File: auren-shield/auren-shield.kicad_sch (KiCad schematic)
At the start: 47 parts, among them J1 Tympan_SJ-3523-SMT-TR, J2 Tympan_SJ-3524-SMT-TR-PI, J3 HDMI_A_Molex_208658-1001, J5 Conn_01x01, J6 Conn_01x01, P1 CONN_01X06, P2 CONN_01X06, P3 CONN_01X06, P4 CONN_01X06, P5 CONN_01X06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

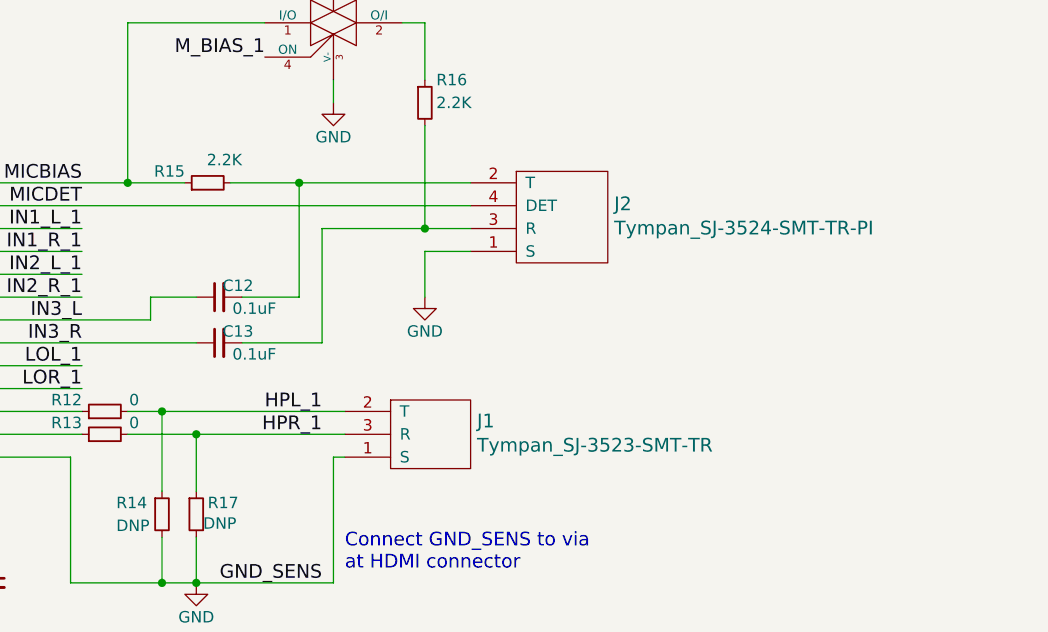
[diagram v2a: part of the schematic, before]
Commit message: Removed audio jacks. Resized PCB
Cleaned up around GND_SNS circuit
PCB is now 38mm x 40mm (was x 44mm)
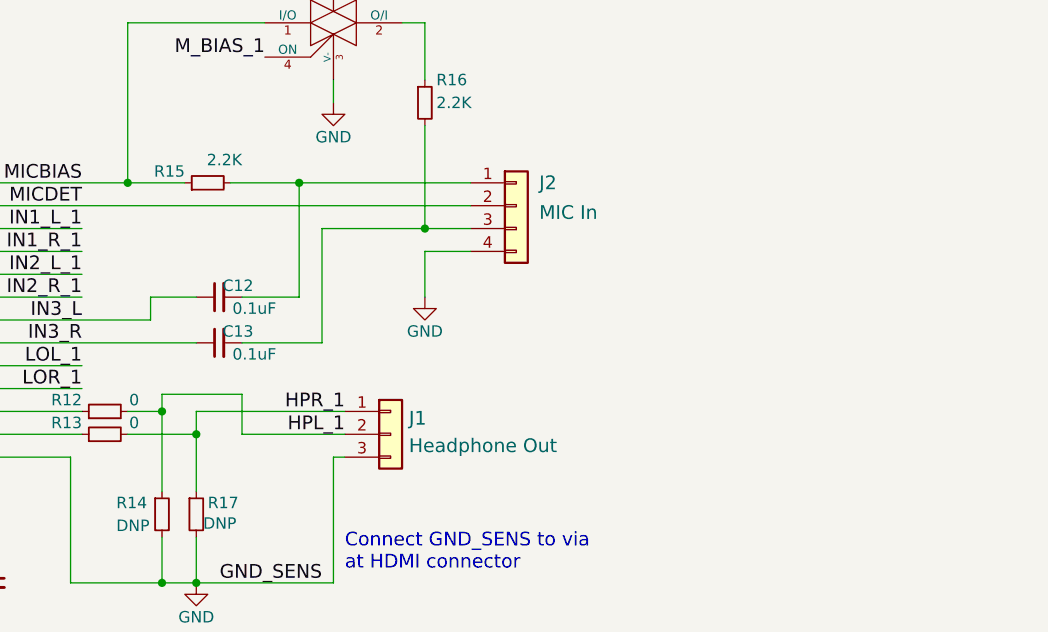
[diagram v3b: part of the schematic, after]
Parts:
- C23: footprint Capacitors_SMD:C_0402 -> Capacitor_SMD:C_0402_1005Metric
- J1: value Tympan_SJ-3523-SMT-TR -> Headphone Out; footprint Tympan:SJ-3523-SMT-TR -> Connector_PinHeader_2.54mm:PinHeader_1x03_P2.54mm_Vertical; symbol auren-shield:Tympan_SJ-3523-SMT-TR -> Connector_Generic:Conn_01x03
- J2: value Tympan_SJ-3524-SMT-TR-PI -> MIC In; footprint Tympan:SJ-3524-SMT-TR -> Connector_PinHeader_2.54mm:PinHeader_1x04_P2.54mm_Vertical; symbol auren-shield:Tympan_SJ-3524-SMT-TR-PI -> Connector_Generic:Conn_01x04
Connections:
- net GND: now also J1.3 (Pin_3), J2.4 (Pin_4); no longer J1.1 (S), J2.1 (S)
- net HPR_1: now also J1.1 (Pin_1); no longer J1.3 (R)
- net MICDET: now also J2.2 (Pin_2); no longer J2.4 (DET)
- net at C12.2, R15.2: now also J2.1 (Pin_1); no longer J2.2 (T)
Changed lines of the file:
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@@
 	)
 	(junction
-		(at 162.56 82.55)
-		(diameter 0)
-		(color 0 0 0 0)
-	)
-	(junction
 		(at 115.57 99.06)
 		(diameter 0)
@@
 	)
 	(junction
-		(at 111.76 99.06)
+		(at 162.56 82.55)
 		(diameter 0)
 		(color 0 0 0 0)
 	)
 	(junction
-		(at 109.22 99.06)
+		(at 111.76 99.06)
 		(diameter 0)
 		(color 0 0 0 0)
@@
 	)
 	(junction
+		(at 109.22 99.06)
+		(diameter 0)
+		(color 0 0 0 0)
+	)
+	(junction
 		(at 162.56 99.06)
 		(diameter 0)
@@
 	(wire
 		(pts
+			(xy 179.07 80.01) (xy 162.56 80.01)
+		)
+		(stroke
+			(width 0)
+			(type default)
+		)
+	)
+	(wire
+		(pts
 			(xy 69.85 69.85) (xy 83.82 69.85)
 		)
@@
 	(wire
 		(pts
-			(xy 110.49 43.18) (xy 113.03 43.18)
+			(xy 167.64 82.55) (xy 167.64 78.105)
 		)
 		(stroke
@@
 	(wire
 		(pts
-			(xy 39.37 72.39) (xy 25.4 72.39)
+			(xy 110.49 43.18) (xy 113.03 43.18)
 		)
 		(stroke
@@
 	(wire
 		(pts
-			(xy 247.65 135.89) (xy 245.11 135.89)
+			(xy 39.37 72.39) (xy 25.4 72.39)
 		)
 		(stroke
@@
 	(wire
 		(pts
-			(xy 176.53 59.69) (xy 187.96 59.69)
+			(xy 247.65 135.89) (xy 245.11 135.89)
 		)
 		(stroke
@@
 	(wire
 		(pts
-			(xy 72.39 59.69) (xy 58.42 59.69)
+			(xy 176.53 59.69) (xy 187.96 59.69)
 		)
 		(stroke
@@
 	(wire
 		(pts
-			(xy 92.71 25.4) (xy 86.36 25.4)
+			(xy 72.39 59.69) (xy 58.42 59.69)
 		)
 		(stroke
@@
 	(wire
 		(pts
-			(xy 162.56 82.55) (xy 179.07 82.55)
+			(xy 92.71 25.4) (xy 86.36 25.4)
 		)
 		(stroke
@@
 	(wire
 		(pts
+			(xy 158.75 78.105) (xy 158.75 80.01)
+		)
+		(stroke
+			(width 0)
+			(type default)
+		)
+	)
+	(wire
+		(pts
 			(xy 116.84 148.59) (xy 113.03 148.59)
 		)
@@
 	(wire
 		(pts
+			(xy 167.64 78.105) (xy 158.75 78.105)
+		)
+		(stroke
+			(width 0)
+			(type default)
+		)
+	)
+	(wire
+		(pts
 			(xy 161.29 139.7) (xy 161.29 140.97)
 		)
@@
 	(wire
 		(pts
+			(xy 162.56 80.01) (xy 162.56 82.55)
+		)
+		(stroke
+			(width 0)
+			(type default)
+		)
+	)
+	(wire
+		(pts
 			(xy 177.8 43.18) (xy 177.8 45.72)
 		)
@@
 	(wire
 		(pts
+			(xy 179.07 82.55) (xy 167.64 82.55)
+		)
+		(stroke
+			(width 0)
+			(type default)
+		)
+	)
+	(wire
+		(pts
 			(xy 125.73 30.48) (xy 125.73 33.02)
 		)
@@
 	(wire
 		(pts
-			(xy 158.75 80.01) (xy 179.07 80.01)
-		)
-		(stroke
-			(width 0)
-			(type default)
-		)
-	)
-	(wire
-		(pts
 			(xy 72.39 54.61) (xy 58.42 54.61)
 		)
@@
 	)
 	(label "HPR_1"
-		(at 176.53 82.55 180)
+		(at 179.07 80.01 180)
 		(effects
 			(font
@@
 	)
 	(label "HPL_1"
-		(at 176.53 80.01 180)
+		(at 179.07 82.55 180)
 		(effects
 			(font
@@
 			)
 		)
-		(property "Footprint" "Capacitors_SMD:C_0402"
+		(property "Footprint" "Capacitor_SMD:C_0402_1005Metric"
 			(at 170.18 134.62 0)
 			(effects
@@
 	)
 	(symbol
-		(lib_id "auren-shield:Tympan_SJ-3524-SMT-TR-PI")
-		(at 208.28 59.69 0)
+		(lib_id "Connector_Generic:Conn_01x04")
+		(at 198.12 57.15 0)
 		(unit 1)
 		(exclude_from_sim no)
@@
 		(dnp no)
 		(property "Reference" "J2"
-			(at 208.9912 56.9468 0)
+			(at 200.66 54.61 0)
 			(effects
 				(font
@@
 			)
 		)
-		(property "Value" "Tympan_SJ-3524-SMT-TR-PI"
-			(at 208.9912 59.6392 0)
+		(property "Value" "MIC In"
+			(at 200.66 57.912 0)
 			(effects
 				(font
@@
 			)
 		)
-		(property "Footprint" "Tympan:SJ-3524-SMT-TR"
-			(at 224.282 62.738 0)
+		(property "Footprint" "Connector_PinHeader_2.54mm:PinHeader_1x04_P2.54mm_Vertical"
+			(at 198.12 57.15 0)
 			(effects
 				(font
-					(size 1.524 1.524)
+					(size 1.27 1.27)
 				)
 				(hide yes)
 			)
 		)
-		(property "Datasheet" ""
-			(at 208.28 59.69 0)
+		(property "Datasheet" "~"
+			(at 198.12 57.15 0)
 			(effects
 				(font
-					(size 1.524 1.524)
+					(size 1.27 1.27)
 				)
 				(hide yes)
 			)
 		)
-		(property "Description" ""
-			(at 208.28 59.69 0)
+		(property "Description" "Generic connector, single row, 01x04, script generated (kicad-library-utils/schlib/autogen/connector/)"
+			(at 198.12 57.15 0)
 			(effects
 				(font
@@
 	)
 	(symbol
-		(lib_id "auren-shield:Tympan_SJ-3523-SMT-TR")
-		(at 187.96 82.55 0)
+		(lib_id "Connector_Generic:Conn_01x03")
+		(at 184.15 82.55 0)
 		(unit 1)
 		(exclude_from_sim no)
@@
 		(dnp no)
 		(property "Reference" "J1"
-			(at 193.7512 81.0768 0)
+			(at 186.182 80.772 0)
 			(effects
 				(font
@@
 			)
 		)
-		(property "Value" "Tympan_SJ-3523-SMT-TR"
-			(at 193.7512 83.7692 0)
+		(property "Value" "Headphone Out"
+			(at 186.182 83.82 0)
 			(effects
 				(font
@@
 			)
 		)
-		(property "Footprint" "Tympan:SJ-3523-SMT-TR"
-			(at 213.614 80.264 0)
+		(property "Footprint" "Connector_PinHeader_2.54mm:PinHeader_1x03_P2.54mm_Vertical"
+			(at 184.15 82.55 0)
 			(effects
 				(font
-					(size 1.524 1.524)
+					(size 1.27 1.27)
 				)
 				(hide yes)
 			)
 		)
-		(property "Datasheet" ""
-			(at 187.96 82.55 0)
+		(property "Datasheet" "~"
+			(at 184.15 82.55 0)
 			(effects
 				(font
-					(size 1.524 1.524)
+					(size 1.27 1.27)
 				)
+				(hide yes)
 			)
 		)
-		(property "Description" ""
-			(at 187.96 82.55 0)
+		(property "Description" "Generic connector, single row, 01x03, script generated (kicad-library-utils/schlib/autogen/connector/)"
+			(at 184.15 82.55 0)
 			(effects
 				(font

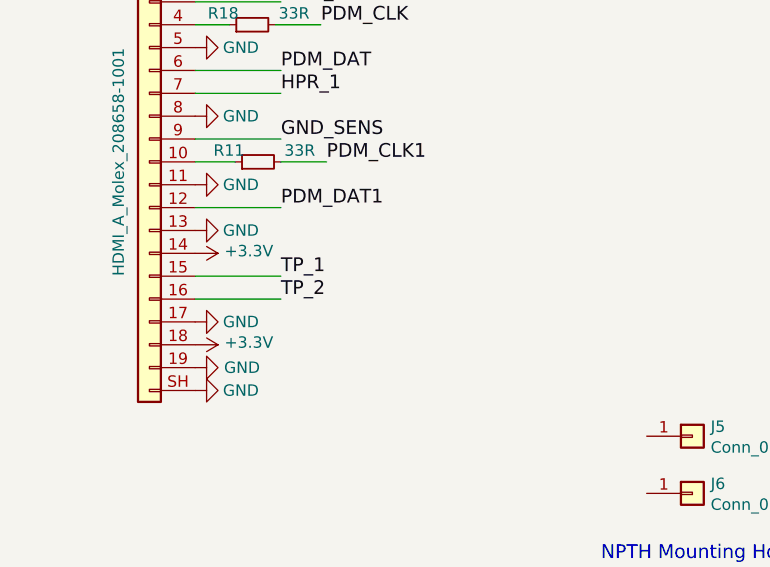
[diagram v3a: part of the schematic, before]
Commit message: Added test point pads
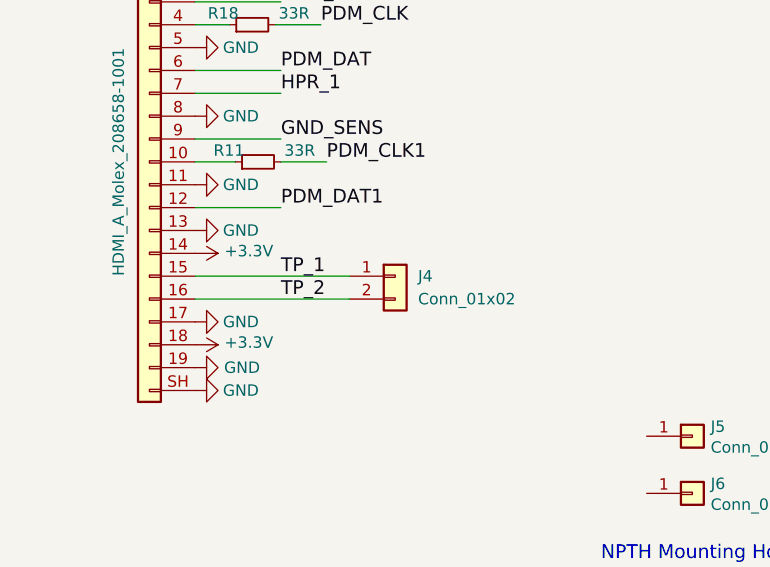
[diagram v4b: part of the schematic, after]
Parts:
- added J4: Conn_01x02, Connector_PinSocket_2.54mm:PinSocket_1x02_P2.54mm_Vertical, symbol Connector_Generic:Conn_01x02
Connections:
- net TP_1: now also J4.1 (Pin_1)
- net TP_2: now also J4.2 (Pin_2)
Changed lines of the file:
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@@
 	(wire
 		(pts
-			(xy 54.61 158.75) (xy 45.085 158.75)
+			(xy 45.085 158.75) (xy 62.23 158.75)
 		)
 		(stroke
@@
 	(wire
 		(pts
-			(xy 54.61 161.29) (xy 45.085 161.29)
+			(xy 45.085 161.29) (xy 62.23 161.29)
 		)
 		(stroke
@@
 					(unit 1)
 				)
+			)
+		)
+	)
+	(symbol
+		(lib_id "Connector_Generic:Conn_01x02")
+		(at 67.31 158.75 0)
+		(unit 1)
+		(exclude_from_sim no)
+		(in_bom yes)
+		(on_board yes)
+		(dnp no)
+		(fields_autoplaced yes)
+		(property "Reference" "J4"
+			(at 69.85 158.7499 0)
+			(effects
+				(font
+					(size 1.27 1.27)
+				)
+				(justify left)
+			)
+		)
+		(property "Value" "Conn_01x02"
+			(at 69.85 161.2899 0)
+			(effects
+				(font
+					(size 1.27 1.27)
+				)
+				(justify left)
+			)
+		)
+		(property "Footprint" "Connector_PinSocket_2.54mm:PinSocket_1x02_P2.54mm_Vertical"
+			(at 67.31 158.75 0)
+			(effects
+				(font
+					(size 1.27 1.27)
+				)
+				(hide yes)
+			)
+		)
+		(property "Datasheet" "~"
+			(at 67.31 158.75 0)
+			(effects
+				(font
+					(size 1.27 1.27)
+				)
+				(hide yes)
+			)
+		)
+		(property "Description" "Generic connector, single row, 01x02, script generated (kicad-library-utils/schlib/autogen/connector/)"
+			(at 67.31 158.75 0)
+			(effects
+				(font
+					(size 1.27 1.27)
+				)
+				(hide yes)
+			)
+		)
+		(pin "1"
+		)
+		(pin "2"
+		)
+		(instances
+			(project ""
+				(path "/2aef2ae4-0dbd-424b-8fd8-1bf240a2e15b"
+					(reference "J4")
+					(unit 1)
+				)

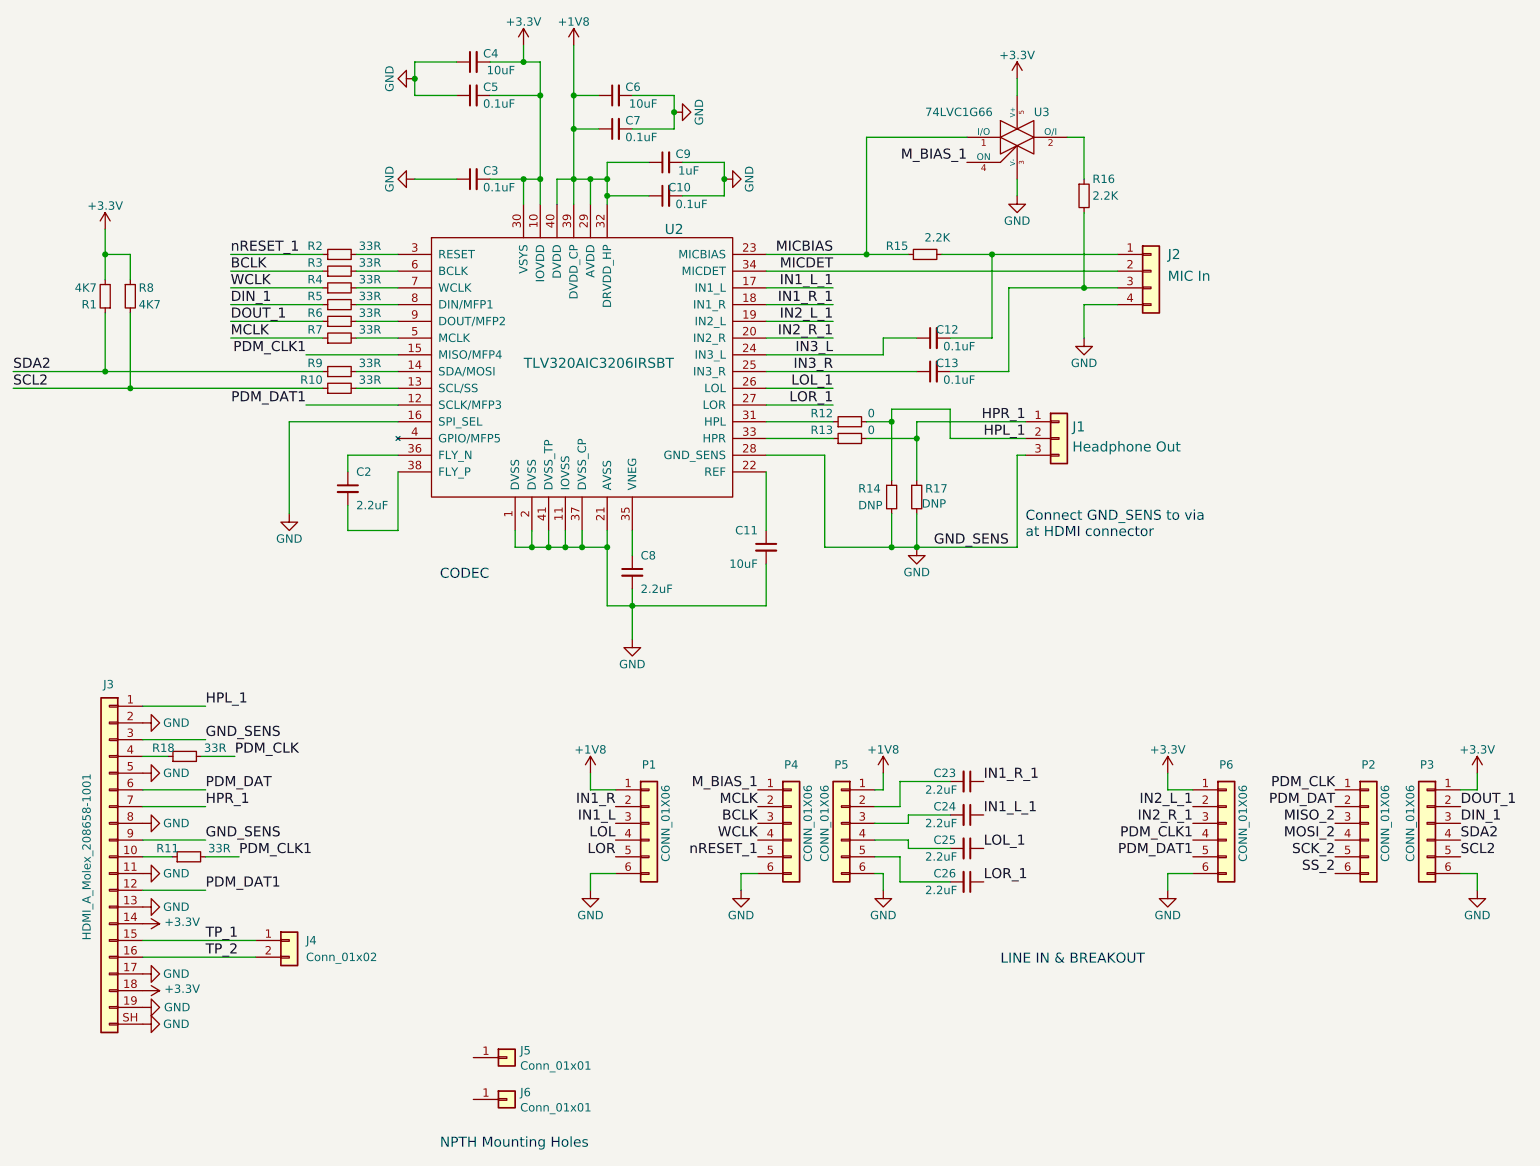
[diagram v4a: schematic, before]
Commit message: Added a step file of the Auren Shield
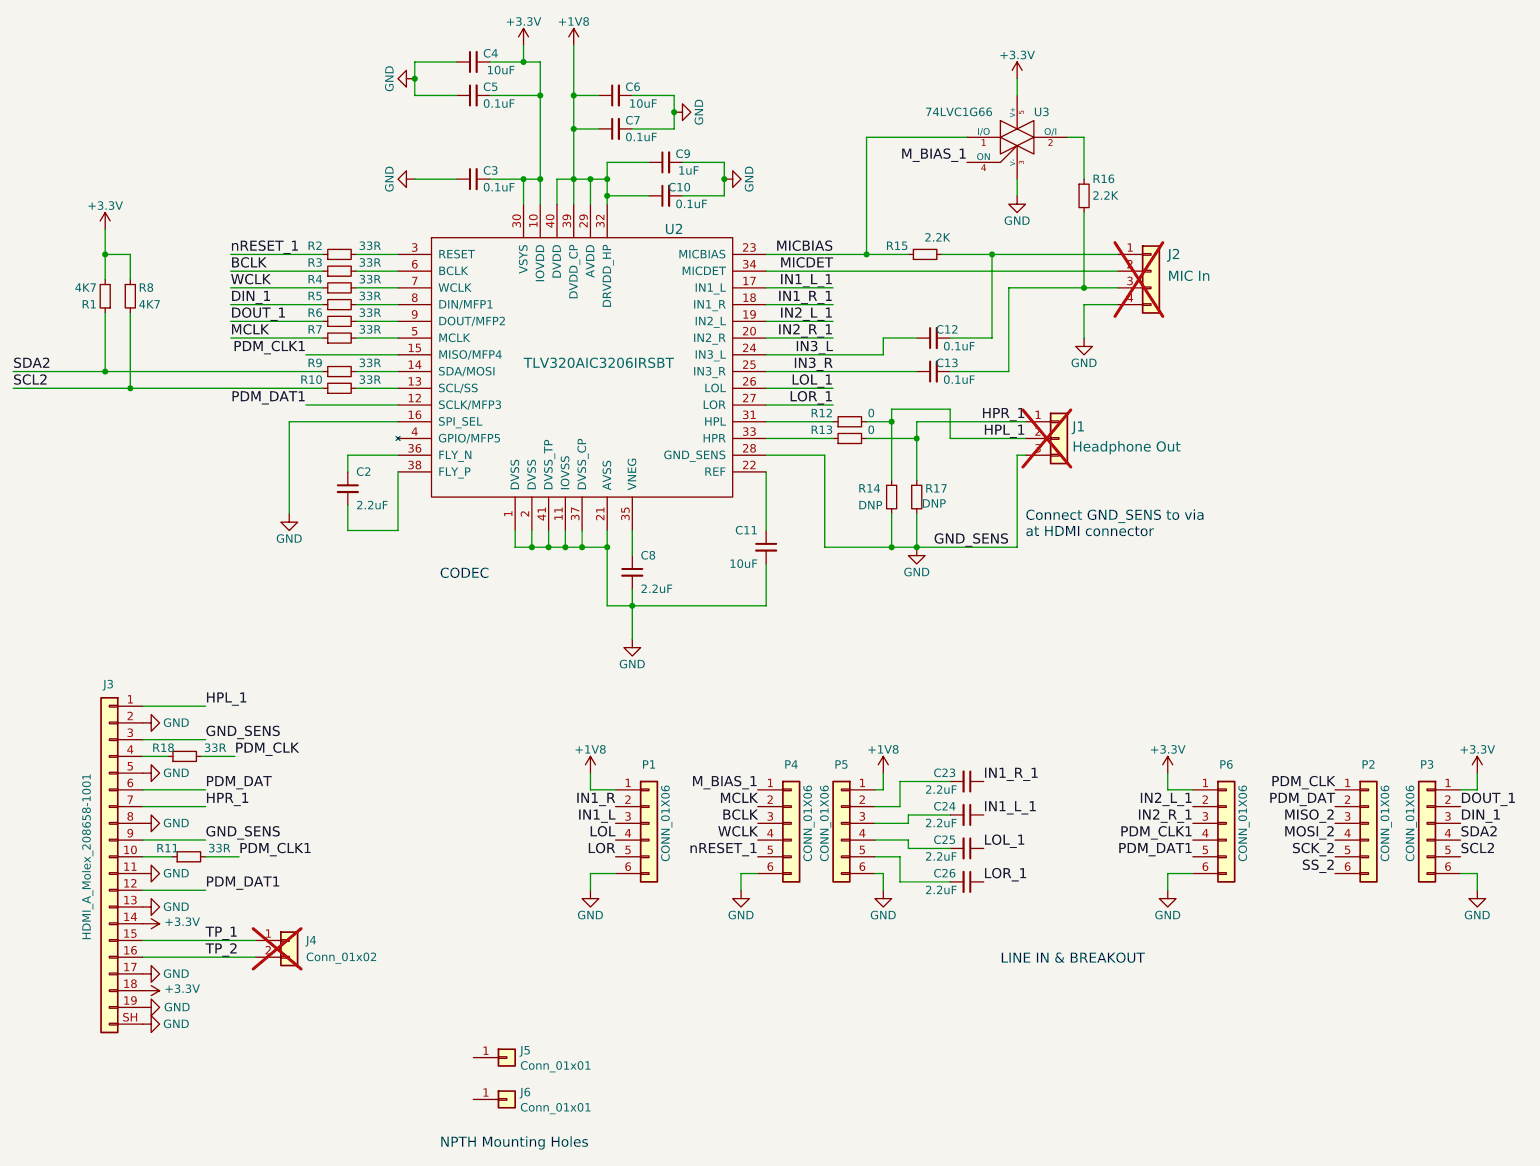
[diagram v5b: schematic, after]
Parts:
- J1, J2, J4: now not fitted; now left out of the parts list
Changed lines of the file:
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@@
 		(unit 1)
 		(exclude_from_sim no)
-		(in_bom yes)
-		(on_board yes)
-		(dnp no)
+		(in_bom no)
+		(on_board yes)
+		(dnp yes)
 		(property "Reference" "J2"
 			(at 200.66 54.61 0)
@@
 		(unit 1)
 		(exclude_from_sim no)
-		(in_bom yes)
-		(on_board yes)
-		(dnp no)
+		(in_bom no)
+		(on_board yes)
+		(dnp yes)
 		(property "Reference" "J1"
 			(at 186.182 80.772 0)
@@
 		(unit 1)
 		(exclude_from_sim no)
-		(in_bom yes)
-		(on_board yes)
-		(dnp no)
+		(in_bom no)
+		(on_board yes)
+		(dnp yes)
 		(fields_autoplaced yes)
 		(property "Reference" "J4"
